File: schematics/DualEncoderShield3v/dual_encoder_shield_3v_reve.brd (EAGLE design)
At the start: 68.6 x 53.3 mm, 21 parts, among them J1 2X6 FEMALE, M1 ARDUINO_R3_ICSP, U1 74LVC1G17W5-7, U3 74LVC1G17W5-7

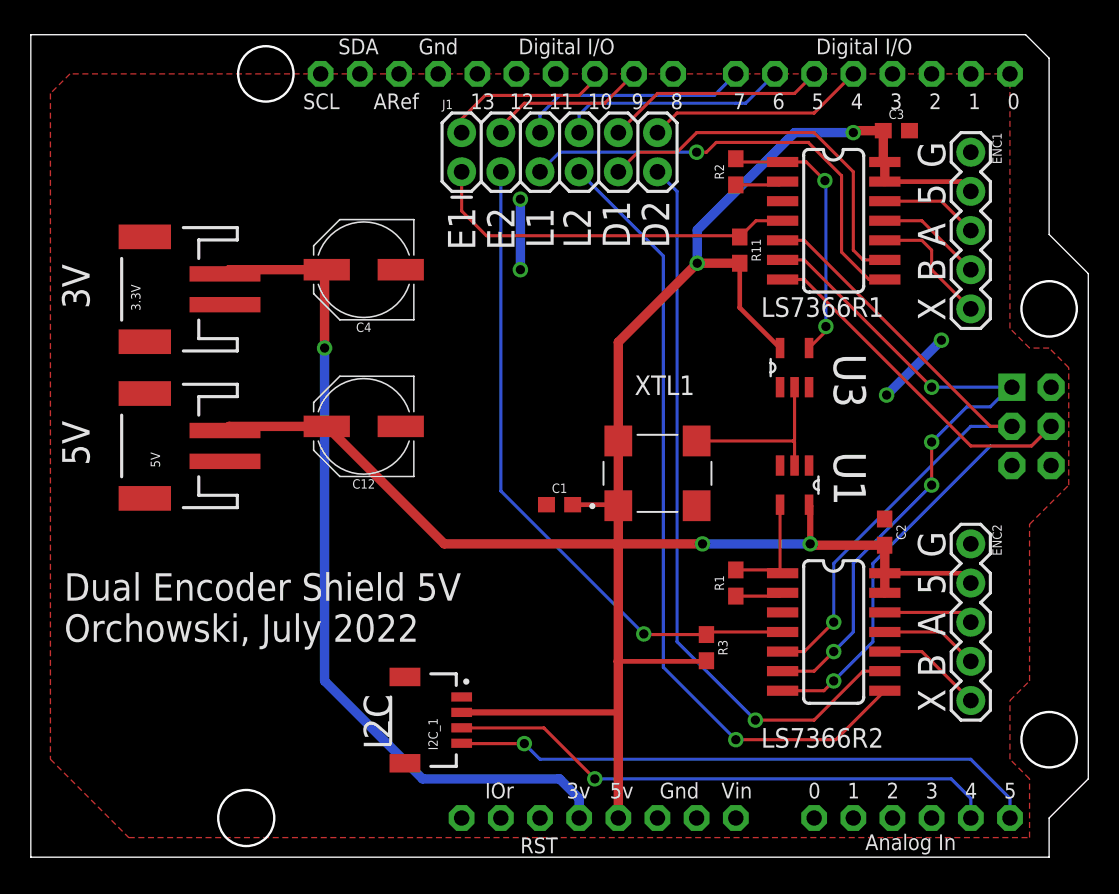
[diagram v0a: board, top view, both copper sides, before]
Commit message: Update readme, sketches, and schematics
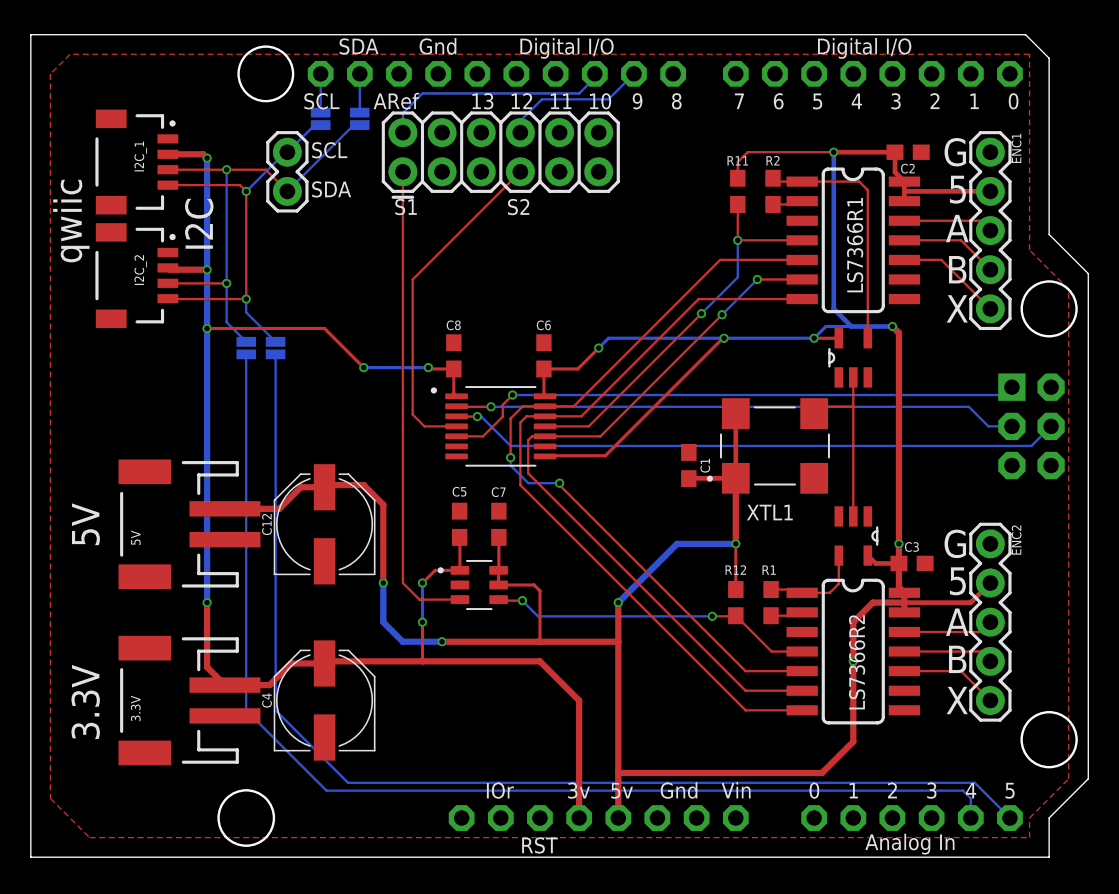
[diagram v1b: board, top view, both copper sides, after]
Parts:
- removed R3: 1k, SparkFun-Resistors:0603
- removed U1: 74LVC1G17W5-7, 74LVC1G17W5-7:SOT95P280X145-5N
- added A4_SDA, A5_SCL, SCL1, SDA1: JUMPER-SMT_2_NO_NO-SILK, SparkFun-Jumpers:SMT-JUMPER_2_NO_NO-SILK
- added C5, C6, C7, C8: 0.1uF, SparkFun-Capacitors:0603
- added I2C_2: (no value), SparkFun-Connectors:JST04_1MM_RA
- added J2: (no value), SparkFun-Connectors:1X02
- added R12: 1k, SparkFun-Resistors:0603
- added TXU1: TXU0304PWR, steveo:SOP65P640X95-14N
- added U$1: TXU0101DBVR, steveo:SOT23-6
- added U4: 74LVC1G17W5-7, 74LVC1G17W5-7:SOT95P280X145-5N
- moved I2C_1 40.9 mm to (8.89, 45.1)
- moved C3 28.1 mm to (57.1, 19.1)
- moved C4 28.1 mm to (19.1, 10.2), turned to 90 degrees
- moved 3.3V 26.7 mm to (8.89, 10.2)
- moved C2 24.7 mm to (56.9, 45.7), turned to 180 degrees
- moved C1 8.76 mm to (42.7, 25.4), turned to 270 degrees
- moved XTL1 7.82 mm to (48.3, 26.7)
- moved C12 6.84 mm to (19.1, 21.6), turned to 90 degrees
- moved 5V 5.08 mm to (8.89, 21.6)
- moved U3 3.86 mm to (53.3, 32.4)
- moved R11 3.81 mm to (45.8, 43.2), turned to 90 degrees
- moved J1 3.81 mm to (24.1, 44.5)
- moved R2 2.73 mm to (48.1, 43.2)
- moved R1 2.62 mm to (48.0, 16.5)
- moved LS7366R1 1.80 mm to (53.3, 39.4)
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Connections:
- removed net ENC1_DFLAG: J1.9, LS7366R1.9
- removed net ENC1_LFLAG: J1.5, LS7366R1.8
- removed net ENC2_DFLAG: J1.11, LS7366R2.9
- removed net ENC2_LFLAG: J1.7, LS7366R2.8
- removed net SS_ENC1: J1.1, LS7366R1.4, R11.1
- removed net SS_ENC2: J1.3, LS7366R2.4, R3.1
- new net ENC_SEL1: J1.7, TXU1.4
- new net ENC_SEL1_5V: LS7366R1.4, R11.1, TXU1.11
- new net ENC_SEL2: J1.1, U$1.3
- new net ENC_SEL2_5V: LS7366R2.4, R12.1, U$1.4
- new net MISO_5V: LS7366R1.6, LS7366R2.6, TXU1.10
- new net MOSI_5V: LS7366R1.7, LS7366R2.7, TXU1.12
- new net SCK_5V: LS7366R1.5, LS7366R2.5, TXU1.13
- new net SCL: A5_SCL.2, I2C_1.4, I2C_2.4, J2.1, SCL1.2
- new net SDA: A4_SDA.2, I2C_1.3, I2C_2.3, J2.2, SDA1.2
- net 3.3V: now also C5.1, C8.1, I2C_1.2, I2C_2.2, TXU1.1, U$1.1
- net 5V: now also C6.1, C7.1, R12.2, TXU1.14, TXU1.8, U$1.5, U$1.6, U4.5; no longer I2C_1.2, R3.2, U1.5
- net A4: now also A4_SDA.1; no longer I2C_1.3
- net A5: now also A5_SCL.1; no longer I2C_1.4
- net CLK: now also U4.2; no longer U1.2
- net GND: now also C5.2, C6.2, C7.2, C8.2, I2C_2.1, TXU1.7, U$1.2, U4.3; no longer U1.3
- net IO4: no longer J1.12
- net IO5: no longer J1.10
- net IO6: no longer J1.8
- net IO7: no longer J1.6
- net MISO: now also TXU1.5; no longer LS7366R1.6, LS7366R2.6
- net MOSI: now also TXU1.3; no longer LS7366R1.7, LS7366R2.7
- net N$8: now also U4.4; no longer U1.4
- net PB1: now also J1.8; no longer J1.4
- net SCK: now also TXU1.2; no longer LS7366R1.5, LS7366R2.5
- net SCL1: now also SCL1.1
- net SDA1: now also SDA1.1
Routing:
- net 5V: track 150.6 -> 211.4 mm, vias 4 -> 11
- net ENC2_LFLAG: track 52.0 -> 0.00 mm, vias 1 -> 0
- net SCK_5V: track 0.00 -> 50.7 mm, vias 0 -> 2
- net MOSI_5V: track 0.00 -> 50.0 mm
- net ENC2_DFLAG: track 47.9 -> 0.00 mm, vias 1 -> 0
- net MISO_5V: track 0.00 -> 47.8 mm, vias 0 -> 2
- net 3.3V: track 54.4 -> 101.1 mm, vias 1 -> 8
- net SS_ENC2: track 42.9 -> 0.00 mm, vias 1 -> 0
- net A4: track 36.2 -> 73.7 mm, vias 1 -> 0
- net A5: track 38.3 -> 73.6 mm, vias 1 -> 0
- net ENC_SEL2: track 0.00 -> 30.8 mm
- net SDA: track 0.00 -> 30.3 mm, vias 0 -> 2
- net ENC1_LFLAG: track 29.7 -> 0.00 mm, vias 1 -> 0
- net SCL: track 0.00 -> 27.5 mm, vias 0 -> 2
- net ENC_SEL1_5V: track 0.00 -> 25.4 mm, vias 0 -> 2
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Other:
- board text added: "3.3V"
- board text added: "Dual Encoder Shield 3.3V, Rev E"
- board text added: "Orchowski, Jan 2023"
- board text added: "S1"
- board text added: "S2"
- board text added: "SCL"
- board text added: "SDA"
- board text added: "qwiic"
- board text removed: "3V"
- board text removed: "D1"
- board text removed: "D2"
- board text removed: "Dual Encoder Shield 5V"
- board text removed: "E1"
- board text removed: "E2"
- board text removed: "L1"
- board text removed: "L2"
- board text removed: "Orchowski, July 2022"
